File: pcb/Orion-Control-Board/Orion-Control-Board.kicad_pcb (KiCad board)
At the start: 2 copper layers, 74.5 x 67.5 mm, 81 parts, among them J1 CONN_20_POS_KEYED_SOCKET, J10 POWER, J2 NUCLEO64_CN7, J3 JETSON_ORIN_NANO_DEVKIT_GPIO, J4 5V Select Socket, J5 5V Select Jumper, J6 NUCLEO64_CN10, J7 I2C 1, J8 I2C 3, J9 UART, U1 BNO055, U2 INA3221, U3 DFR0753 5V BUCK, U4 PCA9685_PWM_SERVO_DRIVER_IC, U5 INA3221, U6 INA3221, Y1 32.768 kHz

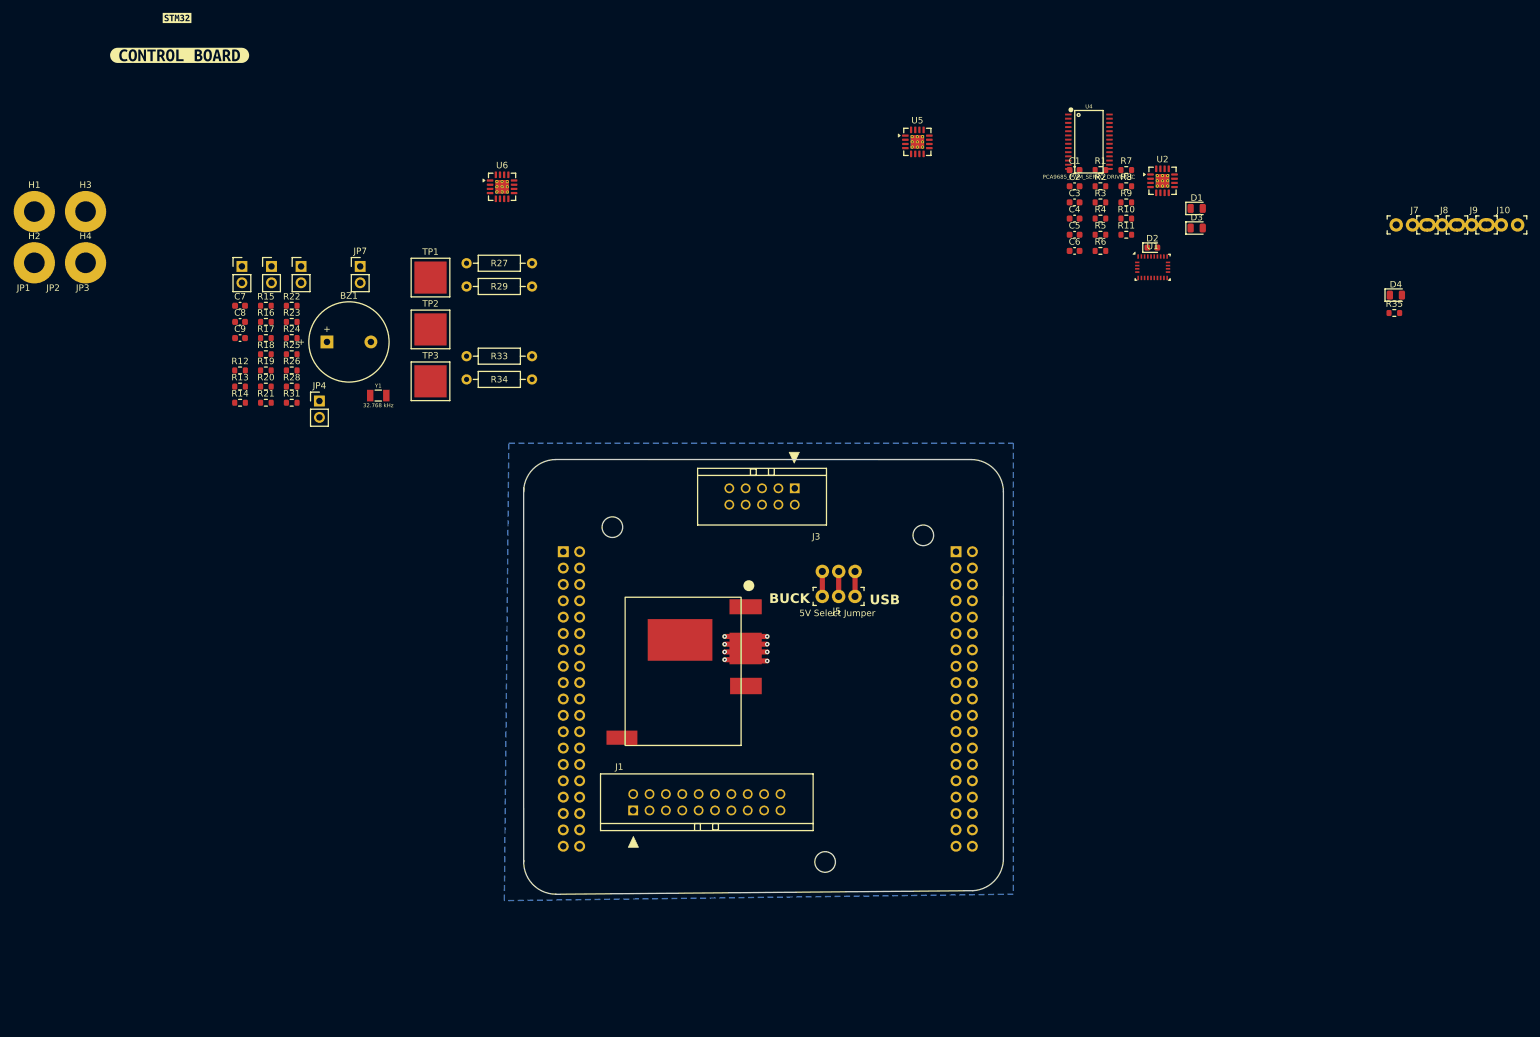
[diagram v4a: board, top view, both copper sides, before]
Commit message: Route IMU and Servo Driver
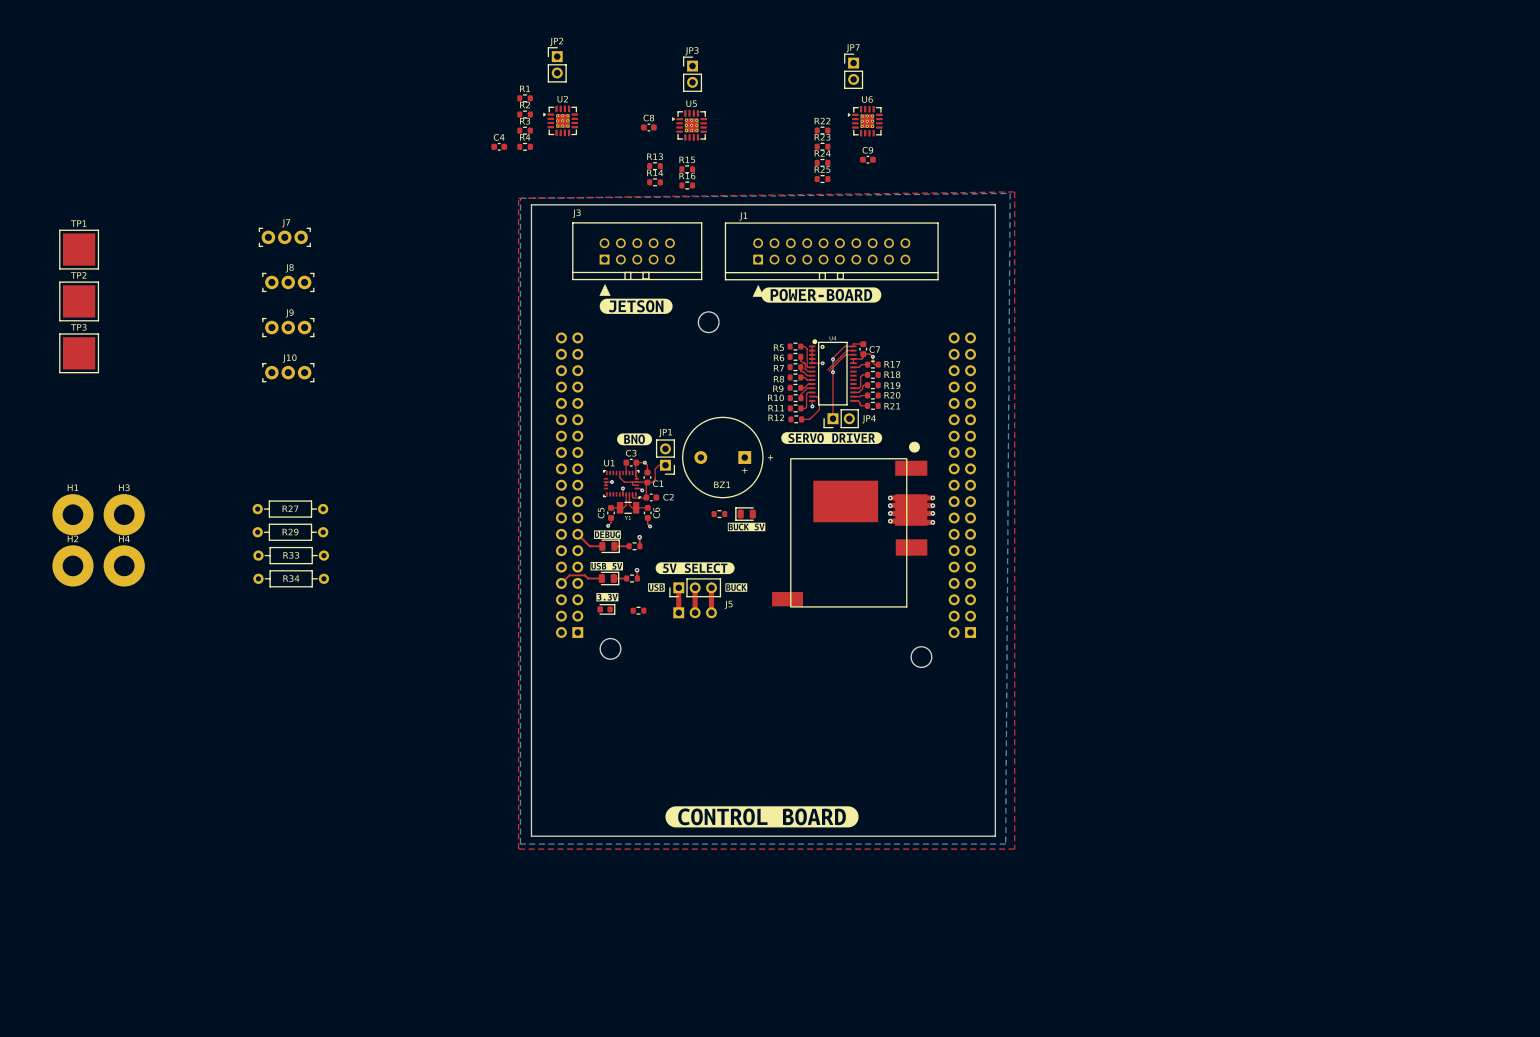
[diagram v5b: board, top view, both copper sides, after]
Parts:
- removed kibuzzard-6742FB76: G***, kibuzzard-6742FB76
- removed kibuzzard-693E4A70: G***, kibuzzard-693E4A70
- added kibuzzard-693EFB08: G***, kibuzzard-693EFB08, F.Cu at (120.5, 70.8)
- added kibuzzard-693EFB23: G***, kibuzzard-693EFB23, F.Cu at (149.2, 69.0)
- added kibuzzard-693EFB3F: G***, kibuzzard-693EFB3F, F.Cu at (116.0, 106.2)
- added kibuzzard-693EFDDB: G***, kibuzzard-693EFDDB, F.Cu at (136.0, 114.4)
- added kibuzzard-693EFDEF: G***, kibuzzard-693EFDEF, F.Cu at (123.6, 114.4)
- added kibuzzard-693EFDF9: G***, kibuzzard-693EFDF9, F.Cu at (129.6, 111.4)
- added kibuzzard-693EFE16: G***, kibuzzard-693EFE16, F.Cu at (150.8, 91.2)
- added kibuzzard-693EFE1D: G***, kibuzzard-693EFE1D, F.Cu at (120.2, 91.4)
- added kibuzzard-693EFF71: G***, kibuzzard-693EFF71, F.Cu at (140.0, 150.0)
- added kibuzzard-693F00A5: G***, kibuzzard-693F00A5, F.Cu at (115.9, 111.1)
- added kibuzzard-693F01AF: G***, kibuzzard-693F01AF, F.Cu at (116.0, 115.9)
- added kibuzzard-693F01CD: G***, kibuzzard-693F01CD, F.Cu at (137.6, 105.0)
- J4: footprint digikey-footprints:PinHeader_1x3_P2.54_Drill1.1mm -> Connector_PinSocket_2.54mm:PinSocket_1x03_P2.54mm_Vertical
- J5: footprint digikey-footprints:PinHeader_1x3_P2.54_Drill1.1mm -> AA_Custom_Components:Jumper_PinHeader_1x03_P2.54mm_Vertical_Bridged
- JP1, JP2, JP3, JP4, JP7: footprint AA_Custom_Components:Jumper_PinHeader_1x02_P2.54mm_Vertical -> AA_Custom_Components:Jumper_PinHeader_1x02_P2.54mm_Vertical_Bridged
- Y1: footprint Clocks:CRYSTAL-SMD-3.2X1.5MM -> AA_Custom_Components:CRYSTAL-SMD-3.2X1.5MM
- moved J10 189.7 mm to (63.9, 81.0)
- moved J9 184.4 mm to (63.9, 74.0)
- moved J8 179.3 mm to (63.9, 67.0)
- moved J7 175.1 mm to (63.4, 60.0)
- moved D4 130.0 mm to (116.1, 113.0), turned to 180 degrees
- moved R35 125.3 mm to (119.8, 113.0)
- moved D3 103.8 mm to (116.1, 108.0), turned to 180 degrees
- moved D2 101.8 mm to (115.7, 117.8), turned to 180 degrees
- moved C9 101.3 mm to (156.4, 48.0)
- moved C7 97.0 mm to (155.7, 77.4), turned to 90 degrees
- moved R17 94.3 mm to (157.2, 79.8), turned to 180 degrees
- moved R18 94.3 mm to (157.2, 81.4), turned to 180 degrees
- moved R19 94.3 mm to (157.2, 83.0), turned to 180 degrees
- moved R20 94.2 mm to (157.2, 84.6), turned to 180 degrees
- moved R21 94.2 mm to (157.2, 86.2), turned to 180 degrees
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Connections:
- net Net-(U1-XIN32) renamed /Y-
- net Net-(U1-XOUT32) renamed /Y+
- C1 pad 2: Net-(JP1-A) -> /3V3_BNO
- C2 pad 1: Net-(JP1-A) -> /3V3_BNO
- J1 pad 13: 3S_BATT_CELL1 -> 3S_BATT_CELL3
- J1 pad 14: 2S_BATT_REAR_CELL1 -> 2S_BATT_FRONT_CELL2
- J1 pad 16: 2S_BATT_REAR_CELL2 -> 2S_BATT_FRONT_CELL1
- J1 pad 17: 3S_BATT_CELL3 -> 3S_BATT_CELL1
- J1 pad 18: 2S_BATT_FRONT_CELL1 -> 2S_BATT_REAR_CELL2
- J1 pad 20: 2S_BATT_FRONT_CELL2 -> 2S_BATT_REAR_CELL1
- JP1 pad 1: Net-(JP1-A) -> /3V3_BNO
- U1 pad 11: +3.3V -> /3V3_BNO
- U1 pad 28: Net-(JP1-A) -> /3V3_BNO
- U1 pad 3: Net-(JP1-A) -> /3V3_BNO
- U1 pad 4: +3.3V -> /3V3_BNO
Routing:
- net GND: track 20.1 -> 46.1 mm, vias 8 -> 19
- net /3V3_BNO: track 0.00 -> 16.3 mm
- net Net-(JP4-A): track 0.00 -> 15.3 mm, vias 0 -> 2
- net +USB_5V: track 0.00 -> 6.98 mm
- net Net-(U4-CH7): track 0.00 -> 6.30 mm
- net SDA_{1}: track 0.00 -> 5.20 mm
- net SCL_{1}: track 0.00 -> 5.02 mm
- net Net-(U4-CH0): track 0.00 -> 4.70 mm
- net LED_DEBUG: track 0.00 -> 4.58 mm
- net /Y-: track 0.00 -> 4.50 mm
- net /Y+: track 0.00 -> 4.40 mm
- net Net-(U4-CH6): track 0.00 -> 3.95 mm
- net Net-(U4-CH11): track 0.00 -> 3.94 mm
- net Net-(U4-CH1): track 0.00 -> 3.51 mm
- net Net-(U4-CH10): track 0.00 -> 2.86 mm
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- added copper zone on F.Cu, net +3.3V
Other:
- board size 74.5 x 67.5 mm -> 72 x 98 mm
- board text removed: "5V Select Jumper"
- board text removed: "BUCK"
- board text removed: "USB"

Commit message: Route more
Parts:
- removed kibuzzard-693EFE16: G***, kibuzzard-693EFE16
- removed kibuzzard-693EFE1D: G***, kibuzzard-693EFE1D
- added kibuzzard-693F1F19: G***, kibuzzard-693F1F19, F.Cu at (117.3, 99.5)
- J9: footprint digikey-footprints:PinHeader_1x3_P2.54_Drill1.1mm -> Connector_PinHeader_2.54mm:PinHeader_1x03_P2.54mm_Vertical
- moved J10 166.6 mm to (214.9, 151.4)
- moved J7 166.6 mm to (214.4, 130.4)
- moved J8 166.6 mm to (214.9, 137.4)
- moved R29 138.2 mm to (196.1, 138.0)
- moved R33 138.2 mm to (196.2, 141.6)
- moved R34 138.2 mm to (196.2, 145.2)
- moved R27 138.1 mm to (195.9, 134.9)
- moved C8 130.1 mm to (111.5, 172.6)
- moved C9 130.1 mm to (145.5, 177.6)
- moved JP3 130.1 mm to (118.2, 163.1)
- moved JP7 130.1 mm to (143.2, 162.6)
- moved R13 130.1 mm to (112.4, 178.6)
- moved R14 130.1 mm to (112.4, 181.1)
- moved R15 130.1 mm to (117.4, 179.1)
- moved R16 130.1 mm to (117.4, 181.6)
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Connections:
- U2 pad 5: +3.3V -> Net-(JP2-A)
- U2 pad 6: SCL_{2} -> SCL_{3}
- U2 pad 7: SDA_{2} -> SDA_{3}
- U5 pad 5: SDA_{2} -> SDA_{3}
- U5 pad 6: SCL_{2} -> SCL_{3}
- U5 pad 7: SDA_{2} -> SDA_{3}
- U6 pad 5: SCL_{2} -> SCL_{3}
- U6 pad 6: SCL_{2} -> SCL_{3}
- U6 pad 7: SDA_{2} -> SDA_{3}
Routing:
- net +5V: track 0.00 -> 33.4 mm
- net UART_{RX}: track 0.00 -> 31.3 mm
- net Net-(JP2-A): track 0.00 -> 30.2 mm
- net UART_{TX}: track 0.00 -> 26.7 mm
- net GND: track 46.1 -> 54.6 mm, vias 19 -> 22
- net Net-(U2-WARNING): track 0.00 -> 3.05 mm
- net Net-(U2-CRITICAL): track 0.00 -> 2.65 mm
- net Net-(D2-K): track 0.00 -> 2.54 mm
- net Net-(D1-K): track 0.00 -> 2.47 mm
- net Net-(U2-TC): track 0.00 -> 1.83 mm
- net Net-(U2-PV): track 0.00 -> 1.82 mm
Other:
- board size 72 x 98 mm -> 70 x 82.4 mm
- rule pad_to_mask_clearance: 0.05 -> 0
- board text added: "GND"
- board text added: "RX"
- board text added: "TX"

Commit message: Route most traces
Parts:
- removed H1, H2, H3, H4: MountingHole, MountingHole:MountingHole_3.2mm_M3_Pad
- added N1: ORION_LOGO, Orion-Logo:Orion-Logo-20mm, F.Cu at (139.7, 91.6)
- J10, J7, J8: footprint digikey-footprints:PinHeader_1x3_P2.54_Drill1.1mm -> Connector_PinHeader_2.54mm:PinHeader_1x03_P2.54mm_Vertical
- moved TP3 154.4 mm to (171.3, 148.7)
- moved TP2 154.0 mm to (171.3, 139.7)
- moved TP1 153.4 mm to (171.3, 130.3)
- moved J7 85.5 mm to (128.9, 130.4), turned to 90 degrees
- moved R34 77.8 mm to (119.4, 133.0), turned to 180 degrees
- moved R33 77.7 mm to (119.4, 130.0), turned to 180 degrees
- moved J8 75.6 mm to (139.7, 130.3), turned to 90 degrees
- moved R29 74.2 mm to (122.2, 131.0), turned to 90 degrees
- moved R27 70.8 mm to (125.2, 131.0), turned to 90 degrees
- moved J10 51.6 mm to (163.7, 145.2)
- moved JP1 36.3 mm to (152.3, 142.8), turned to 0 degrees
- moved C5 34.5 mm to (142.6, 145.5)
- moved U1 34.5 mm to (144.2, 141.0)
- moved C1 34.5 mm to (148.2, 140.0)
- moved C3 34.5 mm to (145.7, 137.7)
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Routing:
- net Net-(BZ1-+): track 0.00 -> 58.1 mm, vias 0 -> 2
- net SDA_{3}: track 0.00 -> 57.9 mm
- net SCL_{3}: track 0.00 -> 56.2 mm, vias 0 -> 3
- net SCL_{1}: track 5.02 -> 55.7 mm
- net SDA_{1}: track 5.20 -> 55.1 mm, vias 0 -> 4
- net PWM7: track 0.00 -> 48.1 mm
- net PWM6: track 0.00 -> 47.7 mm
- net PWM5: track 0.00 -> 40.7 mm
- net PWM4: track 0.00 -> 40.5 mm
- net +5V: track 33.4 -> 68.3 mm, vias 0 -> 2
- net PWM10: track 0.00 -> 34.4 mm
- net PWM3: track 0.00 -> 33.5 mm
- net PWM2: track 0.00 -> 33.2 mm
- net PWM11: track 0.00 -> 31.9 mm, vias 0 -> 2
- net PWM9: track 0.00 -> 29.4 mm
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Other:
- board text added: "3.3V"
- board text added: "E5V"
- board text added: "SCL_{1}"
- board text added: "SCL_{3}"
- board text added: "SDA_{1}"
- board text added: "SDA_{3}"

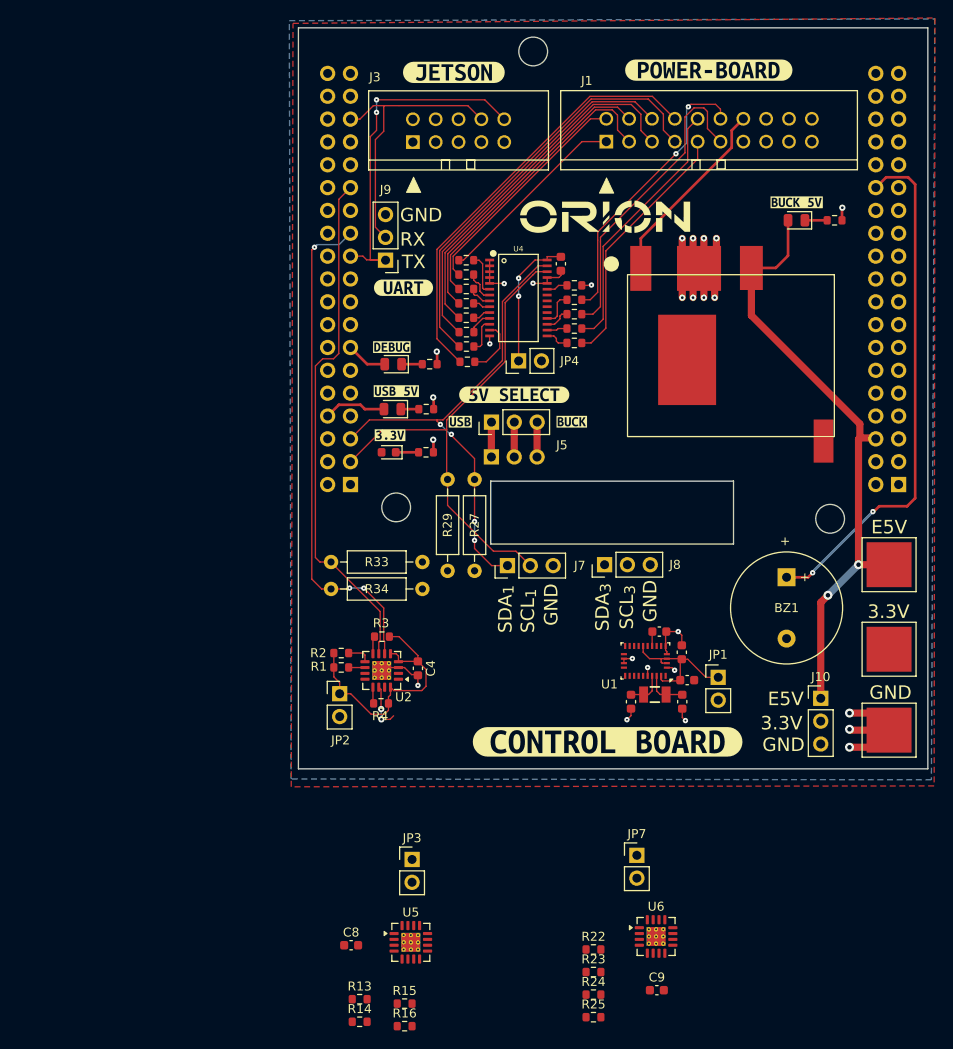
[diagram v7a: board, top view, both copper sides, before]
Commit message: Route all except voltage sensor
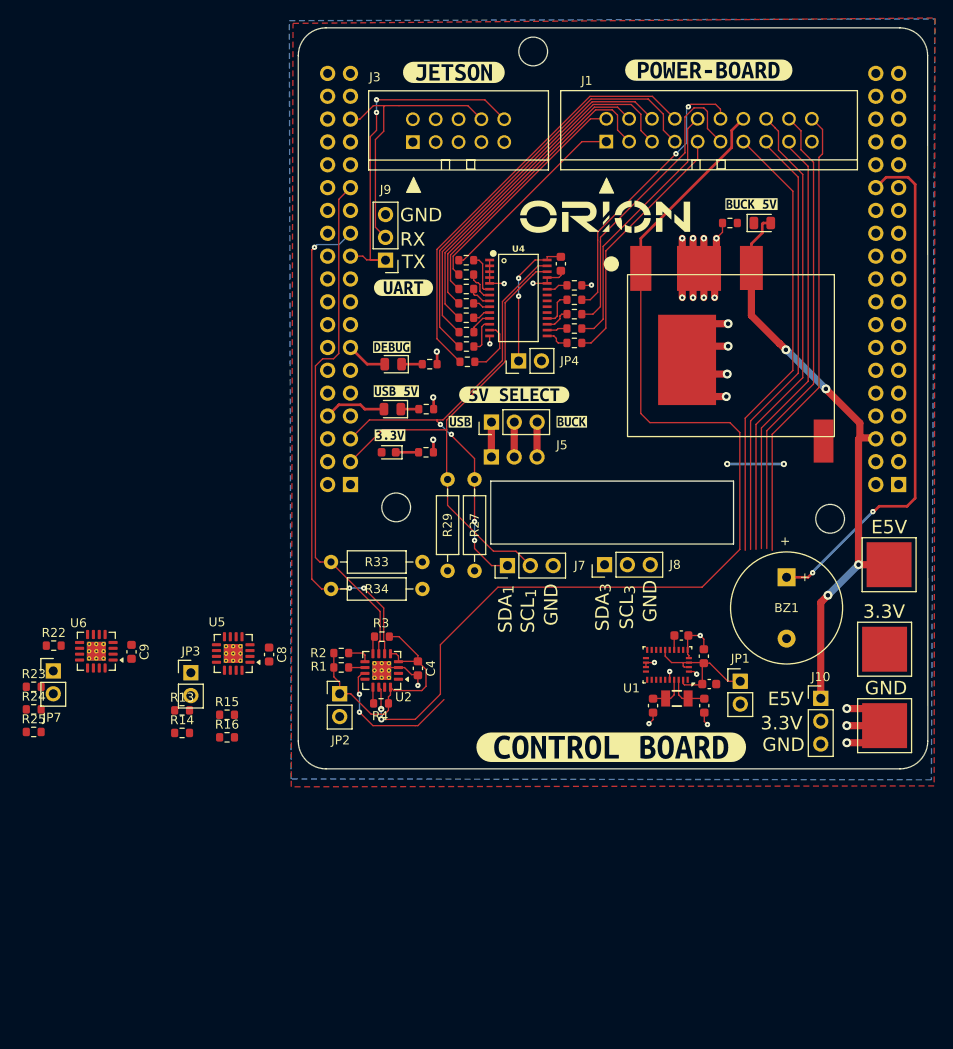
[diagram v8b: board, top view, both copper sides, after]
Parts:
- moved R24 69.9 mm to (76.2, 146.4)
- moved R23 69.9 mm to (76.2, 143.9)
- moved R25 69.9 mm to (76.2, 148.9)
- moved U6 69.9 mm to (83.1, 139.9), turned to 180 degrees
- moved C9 69.5 mm to (87.0, 140.0), turned to -90 degrees
- moved R22 68.9 mm to (78.4, 139.3)
- moved JP7 68.1 mm to (78.3, 142.1)
- moved R13 37.7 mm to (92.7, 146.5)
- moved R14 37.7 mm to (92.7, 149.0)
- moved R15 37.7 mm to (97.7, 147.0)
- moved R16 37.7 mm to (97.7, 149.5)
- moved U5 37.7 mm to (98.4, 140.2), turned to 180 degrees
- moved C8 33.6 mm to (102.3, 140.3), turned to -90 degrees
- moved JP3 32.2 mm to (93.7, 142.3)
- moved R26 11.6 mm to (153.6, 92.3), turned to 180 degrees
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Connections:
- U3 pad 4: unconnected-(U3-THERMAL-Pad4) -> GND
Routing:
- net 2S_BATT_FRONT_CELL2: track 26.6 -> 117.0 mm
- net 2S_BATT_FRONT_CELL1: track 0.00 -> 67.8 mm, vias 0 -> 2
- net 2S_BATT_REAR_CELL2: track 0.00 -> 51.1 mm
- net 2S_BATT_REAR_CELL1: track 0.00 -> 50.8 mm
- net 3S_BATT_CELL3: track 0.00 -> 49.9 mm
- net 3S_BATT_CELL2: track 0.00 -> 49.0 mm
- net 3S_BATT_CELL1: track 0.00 -> 48.3 mm
- net GND: track 69.0 -> 84.1 mm, vias 26 -> 29
- net +3.3V: track 0.00 -> 6.30 mm, vias 0 -> 2
- net Net-(D1-K): track 2.47 -> 0.00 mm
- net +5V: track 68.3 -> 66.2 mm, vias 2 -> 4
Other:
- outline, holes or cut-outs redrawn
